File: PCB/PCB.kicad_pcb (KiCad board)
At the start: 2 copper layers, 208.3 x 169.5 mm, 307 parts, among them J55001 Debug, J60001 ALS, J60003 I2C, SW10001 SW_Push, SW11001 SW_Push, SW13001 SW_Push, SW14001 SW_Push, SW17001 SW_Push, SW18001 SW_Push, SW19001 SW_Push, SW20001 SW_Push, SW2001 SW_Push, SW21001 SW_Push, SW22001 SW_Push, SW23001 SW_Push, SW24001 SW_Push, SW25001 SW_Push, SW26001 SW_Push, SW27001 SW_Push, SW28001 SW_Push, SW30001 SW_Push, SW3001 SW_Push, SW31001 SW_Push, SW33001 SW_Push, SW34001 SW_Push, SW35001 SW_Push, SW36001 SW_Push, SW37001 SW_Push, SW38001 SW_Push, SW39001 SW_Push, SW40001 SW_Push, SW4001 SW_Push, SW41001 SW_Push, SW43001 SW_Push, SW44001 SW_Push, SW45001 SW_Push, SW46001 SW_Push, SW47001 SW_Push, SW48001 SW_Push, SW49001 SW_Push, SW50001 SW_Push, SW5001 SW_Push, SW52001 SW_Push, SW53001 SW_Push, SW56001 SW_Push, SW6001 SW_Push, SW7001 SW_Push, SW9001 SW_Push, U10001 SK6812MINI-E_C5149201, U11001 SK6812MINI-E_C5149201, U13001 SK6812MINI-E_C5149201, U14001 SK6812MINI-E_C5149201, U17001 SK6812MINI-E_C5149201, U18001 SK6812MINI-E_C5149201, U19001 SK6812MINI-E_C5149201, U20001 SK6812MINI-E_C5149201, U2001 SK6812MINI-E_C5149201, U21001 SK6812MINI-E_C5149201, U22001 SK6812MINI-E_C5149201, U23001 SK6812MINI-E_C5149201, U24001 SK6812MINI-E_C5149201, U25001 SK6812MINI-E_C5149201, U26001 SK6812MINI-E_C5149201, U27001 SK6812MINI-E_C5149201, U28001 SK6812MINI-E_C5149201, U30001 SK6812MINI-E_C5149201, U3001 SK6812MINI-E_C5149201, U31001 SK6812MINI-E_C5149201, U33001 SK6812MINI-E_C5149201, U34001 SK6812MINI-E_C5149201, U35001 SK6812MINI-E_C5149201, U36001 SK6812MINI-E_C5149201, U37001 SK6812MINI-E_C5149201, U38001 SK6812MINI-E_C5149201, U39001 SK6812MINI-E_C5149201, U40001 SK6812MINI-E_C5149201, U4001 SK6812MINI-E_C5149201, U41001 SK6812MINI-E_C5149201, U43001 SK6812MINI-E_C5149201, U44001 SK6812MINI-E_C5149201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

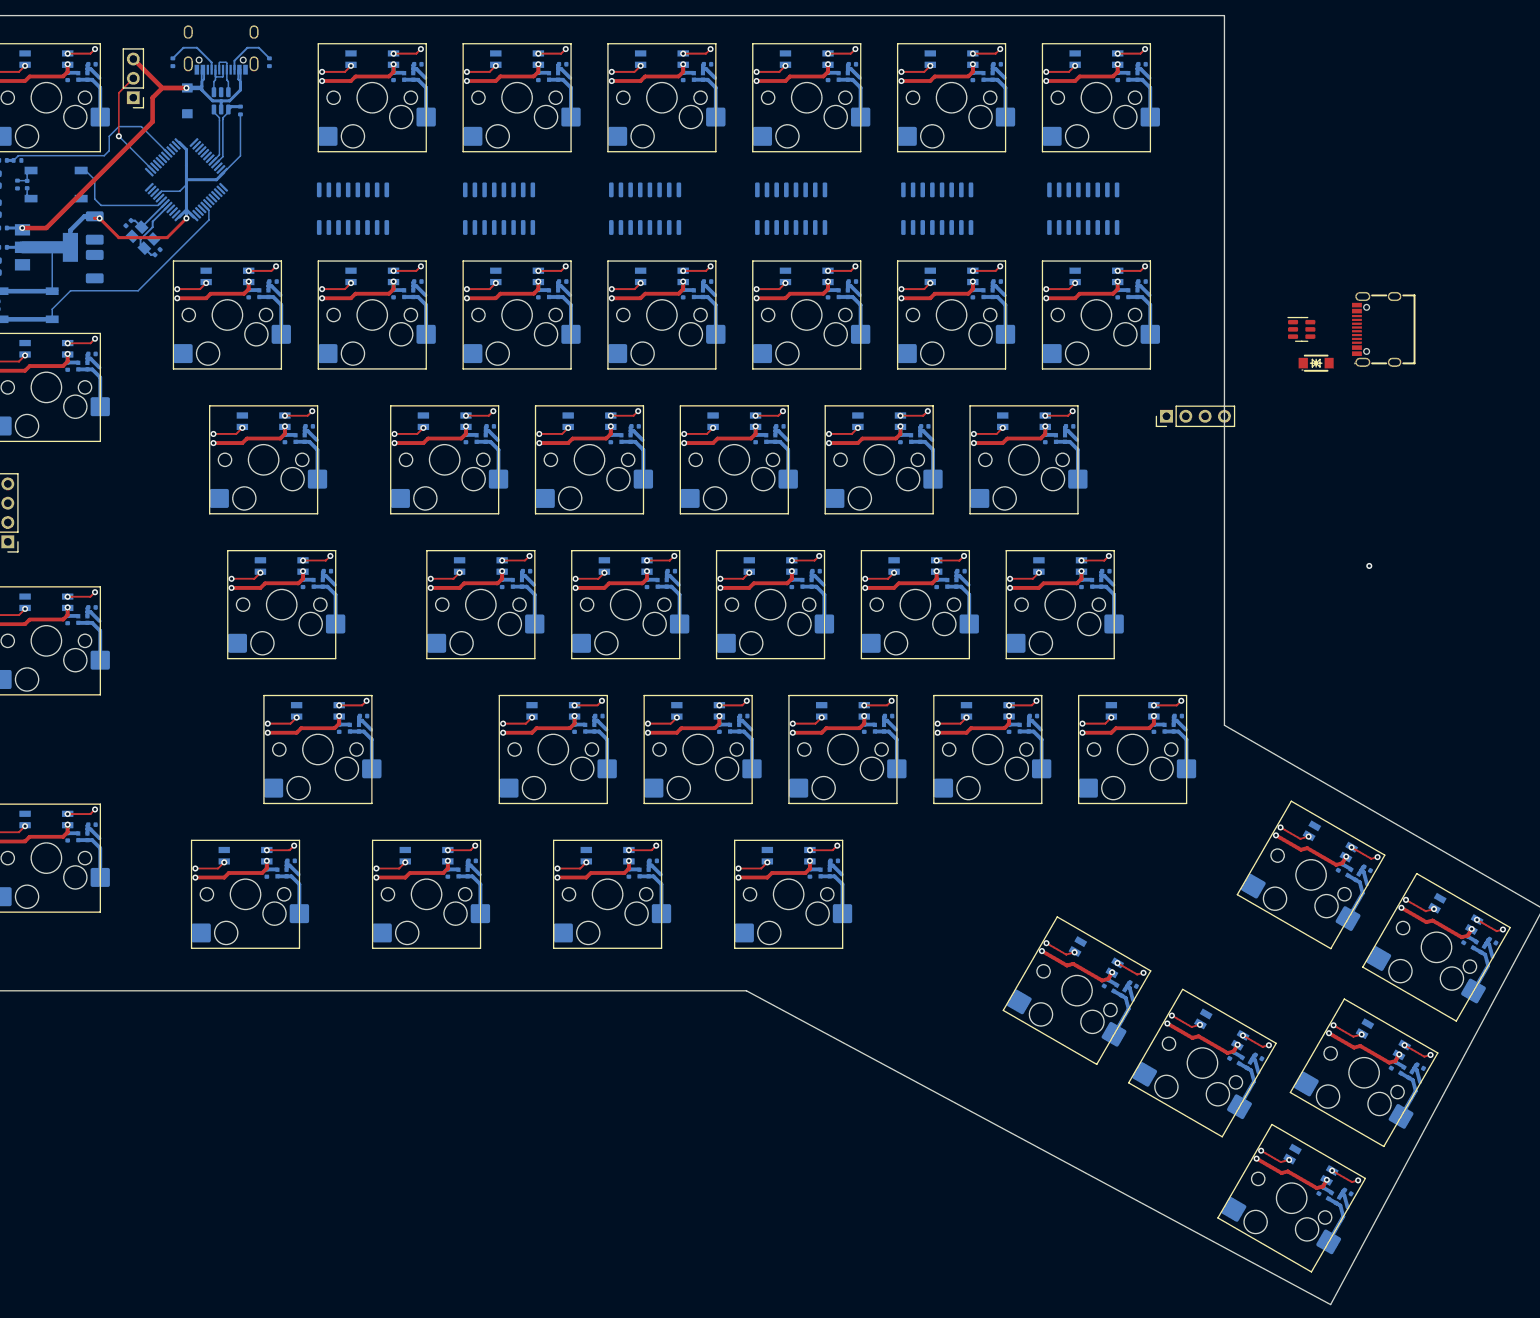
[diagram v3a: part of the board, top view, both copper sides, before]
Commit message: Removed 8-key units, now using the PCB view to handle routing the keys to the SOIP shift registers.
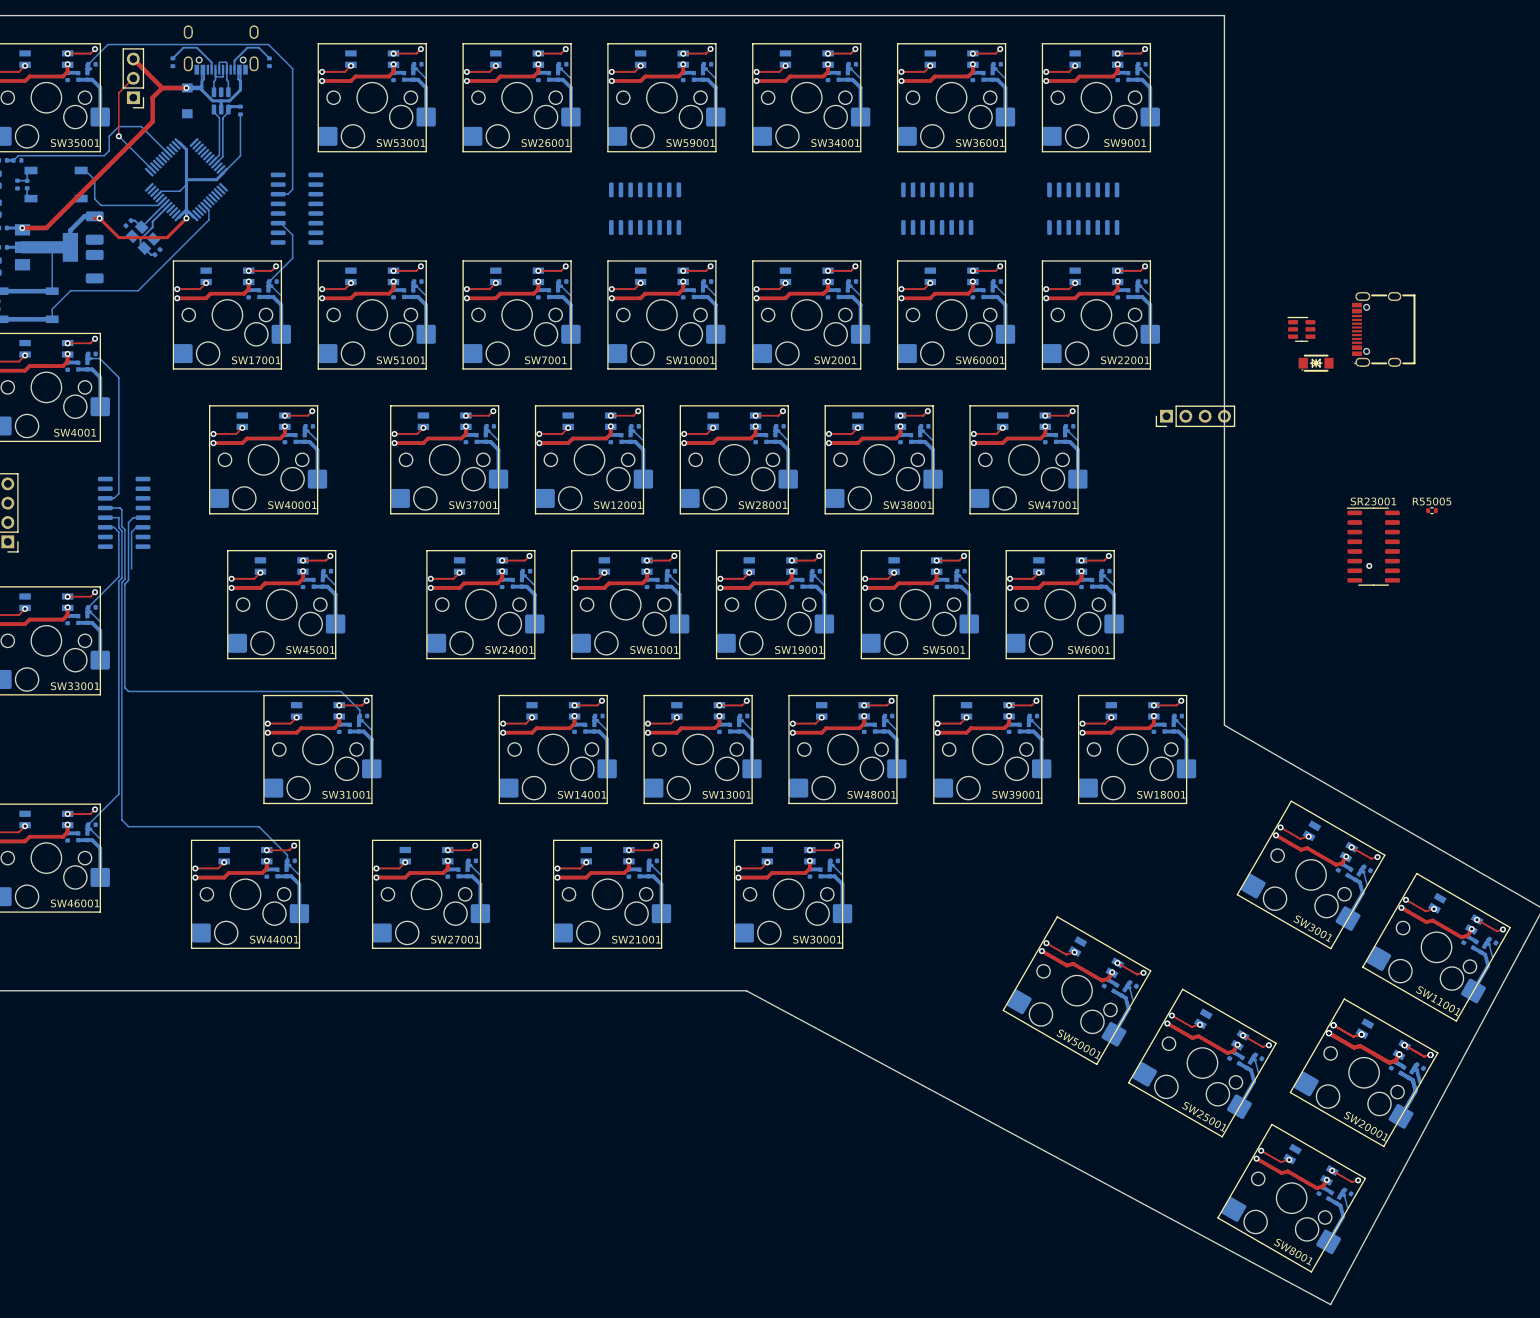
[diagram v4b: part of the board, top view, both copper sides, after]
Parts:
- removed CL23001, CL41001, CL43001, CL49001, CL52001, CL56001, CS23001, CS41001, CS43001, CS49001, CS52001, CS56001: 100nF, Capacitor_SMD:C_0402_1005Metric
- removed RA23001, RA41001, RA43001, RA49001, RA52001, RA56001: 68kΩ, footprint:R0402
- removed RB23001, RB41001, RB43001, RB49001, RB52001, RB56001: 33kΩ, footprint:R0402
- removed SR29001: 74HC165, Package_SO:SOIC-16_3.9x9.9mm_P1.27mm
- removed SW23001, SW41001, SW43001, SW49001, SW52001, SW56001: SW_Push, PCM_Switch_Keyboard_Hotswap_Kailh:SW_Hotswap_Kailh_MX
- removed U23001, U41001, U43001, U49001, U52001, U56001: SK6812MINI-E_C5149201, footprint:LED-SMD_L3.2-W2.8-TR
- added CL12001: 100nF, Capacitor_SMD:C_0402_1005Metric, B.Cu at (104.7, 75.9)
- added CL51001: 100nF, Capacitor_SMD:C_0402_1005Metric, B.Cu at (76.1, 56.9)
- added CL59001: 100nF, Capacitor_SMD:C_0402_1005Metric, B.Cu at (114.2, 28.3)
- added CL60001: 100nF, Capacitor_SMD:C_0402_1005Metric, B.Cu at (152.3, 56.9)
- added CL61001: 100nF, Capacitor_SMD:C_0402_1005Metric, B.Cu at (109.5, 95.0)
- added CL8001: 100nF, Capacitor_SMD:C_0402_1005Metric, B.Cu at (198.1, 174.8)
- added CS12001: 100nF, Capacitor_SMD:C_0402_1005Metric, B.Cu at (107.9, 74.3)
- added CS51001: 100nF, Capacitor_SMD:C_0402_1005Metric, B.Cu at (79.3, 55.3)
- added CS59001: 100nF, Capacitor_SMD:C_0402_1005Metric, B.Cu at (117.4, 26.7)
- added CS60001: 100nF, Capacitor_SMD:C_0402_1005Metric, B.Cu at (155.5, 55.3)
- added CS61001: 100nF, Capacitor_SMD:C_0402_1005Metric, B.Cu at (112.7, 93.4)
- added CS8001: 100nF, Capacitor_SMD:C_0402_1005Metric, B.Cu at (201.7, 175.1)
- added R55005: 5.1k, Resistor_SMD:R_0402_1005Metric, F.Cu at (212.7, 85.4)
- added RA12001: 68kΩ, footprint:R0402, B.Cu at (106.1, 75.9)
- added RA51001: 68kΩ, footprint:R0402, B.Cu at (77.5, 56.9)
- added RA59001: 68kΩ, footprint:R0402, B.Cu at (115.6, 28.3)
- added RA60001: 68kΩ, footprint:R0402, B.Cu at (153.7, 56.9)
- added RA61001: 68kΩ, footprint:R0402, B.Cu at (110.9, 95.0)
- added RA8001: 68kΩ, footprint:R0402, B.Cu at (199.3, 175.5)
- added RB12001: 33kΩ, footprint:R0402, B.Cu at (107.3, 75.9)
- added RB51001: 33kΩ, footprint:R0402, B.Cu at (78.7, 56.9)
- added RB59001: 33kΩ, footprint:R0402, B.Cu at (116.8, 28.3)
- added RB60001: 33kΩ, footprint:R0402, B.Cu at (154.9, 56.9)
- added RB61001: 33kΩ, footprint:R0402, B.Cu at (112.1, 95.0)
- added RB8001: 33kΩ, footprint:R0402, B.Cu at (200.3, 176.1)
- added SR23001: 74HC165, Package_SO:SOIC-16_3.9x9.9mm_P1.27mm, F.Cu at (205.0, 90.2)
- added SW12001: SW_Push, PCM_Switch_Keyboard_Hotswap_Kailh:SW_Hotswap_Kailh_MX, F.Cu at (101.9, 78.7)
- added SW51001: SW_Push, PCM_Switch_Keyboard_Hotswap_Kailh:SW_Hotswap_Kailh_MX, F.Cu at (73.3, 59.7)
- added SW59001: SW_Push, PCM_Switch_Keyboard_Hotswap_Kailh:SW_Hotswap_Kailh_MX, F.Cu at (111.4, 31.1)
- added SW60001: SW_Push, PCM_Switch_Keyboard_Hotswap_Kailh:SW_Hotswap_Kailh_MX, F.Cu at (149.5, 59.7)
- added SW61001: SW_Push, PCM_Switch_Keyboard_Hotswap_Kailh:SW_Hotswap_Kailh_MX, F.Cu at (106.7, 97.8)
- added SW8001: SW_Push, PCM_Switch_Keyboard_Hotswap_Kailh:SW_Hotswap_Kailh_MX, F.Cu at (194.3, 175.9)
- added U12001: SK6812MINI-E_C5149201, footprint:LED-SMD_L3.2-W2.8-TR, B.Cu at (101.9, 73.7)
- added U51001: SK6812MINI-E_C5149201, footprint:LED-SMD_L3.2-W2.8-TR, B.Cu at (73.3, 54.6)
- added U59001: SK6812MINI-E_C5149201, footprint:LED-SMD_L3.2-W2.8-TR, B.Cu at (111.4, 26.0)
- added U60003: SK6812MINI-E_C5149201, footprint:LED-SMD_L3.2-W2.8-TR, B.Cu at (149.5, 54.6)
- added U61001: SK6812MINI-E_C5149201, footprint:LED-SMD_L3.2-W2.8-TR, B.Cu at (106.7, 92.7)
- added U8001: SK6812MINI-E_C5149201, footprint:LED-SMD_L3.2-W2.8-TR, B.Cu at (196.8, 171.5)
- R55006: value 7.7k -> 5.1k
- moved CS4001 198.3 mm to (36.5, 64.8), turned to 180 degrees
- moved U4001 197.9 mm to (30.5, 64.1), turned to 0 degrees
- moved RB4001 197.4 mm to (35.9, 66.4), turned to -90 degrees
- moved RA4001 197.3 mm to (34.7, 66.4), turned to 90 degrees
- moved CL4001 197.1 mm to (33.3, 66.4), turned to 90 degrees
- moved SW4001 195.4 mm to (30.5, 69.2), turned to 180 degrees
- moved U3001 168.9 mm to (199.4, 128.9), turned to -30 degrees
- moved CS3001 167.8 mm to (204.2, 132.5), turned to 150 degrees
- moved CL3001 167.4 mm to (200.6, 132.3), turned to 60 degrees
- moved RA3001 167.2 mm to (201.9, 133.0), turned to 60 degrees
- moved RB3001 167.1 mm to (202.9, 133.6), turned to -120 degrees
- moved SW3001 166.4 mm to (196.8, 133.3), turned to 150 degrees
- moved U20001 146.6 mm to (206.3, 155.0), turned to -30 degrees
- moved CS20001 146.4 mm to (211.2, 158.6), turned to 150 degrees
- moved RB20001 145.6 mm to (209.9, 159.6), turned to -120 degrees
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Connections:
- net /Left Half/5-Key Module/SR_CLOCK renamed /Left Half/8-Key Module/SR_CLOCK
- net /Left Half/5-Key Module/SR_LOAD renamed /Left Half/8-Key Module/SR_LOAD
- CS10001 pad 2: /Left Half/8-Key Module4/Key Unit1/SwitchOutput -> /Left Half/Key Unit16/SwitchOutput
- CS11001 pad 2: /Left Half/8-Key Module1/Key Unit6/SwitchOutput -> /Left Half/Key Unit20/SwitchOutput
- CS13001 pad 2: /Left Half/8-Key Module3/Key Unit4/SwitchOutput -> /Left Half/Key Unit18/SwitchOutput
- CS14001 pad 2: /Left Half/8-Key Module/Key Unit7/SwitchOutput -> /Left Half/Key Unit14/SwitchOutput
- CS17001 pad 2: /Left Half/8-Key Module3/Key Unit3/SwitchOutput -> /Left Half/Key Unit15/SwitchOutput
- CS18001 pad 2: /Left Half/8-Key Module3/Key Unit5/SwitchOutput -> /Left Half/Key Unit11/SwitchOutput
- CS19001 pad 2: /Left Half/8-Key Module4/Key Unit4/SwitchOutput -> /Left Half/Key Unit17/SwitchOutput
- CS20001 pad 2: /Left Half/8-Key Module3/Key Unit2/SwitchOutput -> /Left Half/Key Unit24/SwitchOutput
- CS2001 pad 2: /Left Half/8-Key Module1/Key Unit7/SwitchOutput -> /Left Half/Key Unit6/SwitchOutput
- CS21001 pad 2: /Left Half/8-Key Module2/Key Unit5/SwitchOutput -> /Left Half/Key Unit23/SwitchOutput
- CS22001 pad 2: /Left Half/8-Key Module4/Key Unit5/SwitchOutput -> /Left Half/Key Unit22/SwitchOutput
- CS24001 pad 2: /Left Half/8-Key Module1/Key Unit5/SwitchOutput -> /Left Half/Key Unit25/SwitchOutput
- CS25001 pad 2: /Left Half/8-Key Module/Key Unit5/SwitchOutput -> /Left Half/Key Unit27/SwitchOutput
- CS26001 pad 2: /Left Half/8-Key Module1/Key Unit4/SwitchOutput -> /Left Half/Key Unit21/SwitchOutput
- CS27001 pad 2: /Left Half/8-Key Module4/Key Unit0/SwitchOutput -> /Left Half/Key Unit26/SwitchOutput
- CS28001 pad 2: /Left Half/8-Key Module3/Key Unit6/SwitchOutput -> /Left Half/Key Unit28/SwitchOutput
- CS30001 pad 2: /Left Half/8-Key Module2/Key Unit2/SwitchOutput -> /Left Half/Key Unit30/SwitchOutput
- CS3001 pad 2: /Left Half/8-Key Module4/Key Unit3/SwitchOutput -> /Left Half/Key Unit7/SwitchOutput
- CS31001 pad 2: /Left Half/8-Key Module2/Key Unit1/SwitchOutput -> /Left Half/Key Unit34/SwitchOutput
- CS33001 pad 2: /Left Half/8-Key Module3/Key Unit7/SwitchOutput -> /Left Half/Key Unit33/SwitchOutput
- CS34001 pad 2: /Left Half/8-Key Module1/Key Unit3/SwitchOutput -> /Left Half/Key Unit35/SwitchOutput
- CS35001 pad 2: /Left Half/8-Key Module4/Key Unit6/SwitchOutput -> /Left Half/8-Key Module2/SWIN1
- CS36001 pad 2: /Left Half/8-Key Module3/Key Unit1/SwitchOutput -> /Left Half/Key Unit29/SwitchOutput
- CS37001 pad 2: /Left Half/8-Key Module2/Key Unit3/SwitchOutput -> /Left Half/Key Unit32/SwitchOutput
- CS38001 pad 2: /Left Half/8-Key Module/Key Unit3/SwitchOutput -> /Left Half/Key Unit36/SwitchOutput
- CS39001 pad 2: /Left Half/8-Key Module2/Key Unit4/SwitchOutput -> /Left Half/Key Unit37/SwitchOutput
- CS40001 pad 2: /Left Half/8-Key Module/Key Unit0/SwitchOutput -> /Left Half/Key Unit42/SwitchOutput
- CS4001 pad 2: /Left Half/8-Key Module/Key Unit2/SwitchOutput -> /Left Half/Key Unit3/SwitchOutput
- CS44001 pad 2: /Left Half/8-Key Module3/Key Unit0/SwitchOutput -> /Left Half/Key Unit43/SwitchOutput
- CS45001 pad 2: /Left Half/8-Key Module1/Key Unit1/SwitchOutput -> /Left Half/Key Unit44/SwitchOutput
- CS46001 pad 2: /Left Half/8-Key Module2/Key Unit7/SwitchOutput -> /Left Half/Key Unit38/SwitchOutput
- CS47001 pad 2: /Left Half/8-Key Module4/Key Unit7/SwitchOutput -> /Left Half/Key Unit39/SwitchOutput
- CS48001 pad 2: /Left Half/8-Key Module4/Key Unit2/SwitchOutput -> /Left Half/Key Unit41/SwitchOutput
- CS50001 pad 2: /Left Half/8-Key Module/Key Unit6/SwitchOutput -> /Left Half/Key Unit40/SwitchOutput
- CS5001 pad 2: /Left Half/8-Key Module2/Key Unit6/SwitchOutput -> /Left Half/Key Unit1/SwitchOutput
- CS53001 pad 2: /Left Half/8-Key Module1/Key Unit2/SwitchOutput -> /Left Half/Key Unit45/SwitchOutput
- CS6001 pad 2: /Left Half/8-Key Module2/Key Unit0/SwitchOutput -> /Left Half/Key Unit5/SwitchOutput
- CS7001 pad 2: /Left Half/8-Key Module1/Key Unit0/SwitchOutput -> /Left Half/Key Unit4/SwitchOutput
- CS9001 pad 2: /Left Half/8-Key Module/Key Unit1/SwitchOutput -> /Left Half/Key Unit0/SwitchOutput
- R55006 pad 1: +5V -> Net-(R55005-Pad2)
- RB10001 pad 1: /Left Half/8-Key Module4/Key Unit1/SwitchOutput -> /Left Half/Key Unit16/SwitchOutput
- RB11001 pad 1: /Left Half/8-Key Module1/Key Unit6/SwitchOutput -> /Left Half/Key Unit20/SwitchOutput
- RB13001 pad 1: /Left Half/8-Key Module3/Key Unit4/SwitchOutput -> /Left Half/Key Unit18/SwitchOutput
- RB14001 pad 1: /Left Half/8-Key Module/Key Unit7/SwitchOutput -> /Left Half/Key Unit14/SwitchOutput
- RB17001 pad 1: /Left Half/8-Key Module3/Key Unit3/SwitchOutput -> /Left Half/Key Unit15/SwitchOutput
- RB18001 pad 1: /Left Half/8-Key Module3/Key Unit5/SwitchOutput -> /Left Half/Key Unit11/SwitchOutput
- RB19001 pad 1: /Left Half/8-Key Module4/Key Unit4/SwitchOutput -> /Left Half/Key Unit17/SwitchOutput
- RB20001 pad 1: /Left Half/8-Key Module3/Key Unit2/SwitchOutput -> /Left Half/Key Unit24/SwitchOutput
- RB2001 pad 1: /Left Half/8-Key Module1/Key Unit7/SwitchOutput -> /Left Half/Key Unit6/SwitchOutput
- RB21001 pad 1: /Left Half/8-Key Module2/Key Unit5/SwitchOutput -> /Left Half/Key Unit23/SwitchOutput
- RB22001 pad 1: /Left Half/8-Key Module4/Key Unit5/SwitchOutput -> /Left Half/Key Unit22/SwitchOutput
- RB24001 pad 1: /Left Half/8-Key Module1/Key Unit5/SwitchOutput -> /Left Half/Key Unit25/SwitchOutput
- RB25001 pad 1: /Left Half/8-Key Module/Key Unit5/SwitchOutput -> /Left Half/Key Unit27/SwitchOutput
- RB26001 pad 1: /Left Half/8-Key Module1/Key Unit4/SwitchOutput -> /Left Half/Key Unit21/SwitchOutput
- RB27001 pad 1: /Left Half/8-Key Module4/Key Unit0/SwitchOutput -> /Left Half/Key Unit26/SwitchOutput
- RB28001 pad 1: /Left Half/8-Key Module3/Key Unit6/SwitchOutput -> /Left Half/Key Unit28/SwitchOutput
- RB30001 pad 1: /Left Half/8-Key Module2/Key Unit2/SwitchOutput -> /Left Half/Key Unit30/SwitchOutput
- RB3001 pad 1: /Left Half/8-Key Module4/Key Unit3/SwitchOutput -> /Left Half/Key Unit7/SwitchOutput
- RB31001 pad 1: /Left Half/8-Key Module2/Key Unit1/SwitchOutput -> /Left Half/Key Unit34/SwitchOutput
- RB33001 pad 1: /Left Half/8-Key Module3/Key Unit7/SwitchOutput -> /Left Half/Key Unit33/SwitchOutput
- RB34001 pad 1: /Left Half/8-Key Module1/Key Unit3/SwitchOutput -> /Left Half/Key Unit35/SwitchOutput
- RB35001 pad 1: /Left Half/8-Key Module4/Key Unit6/SwitchOutput -> /Left Half/8-Key Module2/SWIN1
- RB36001 pad 1: /Left Half/8-Key Module3/Key Unit1/SwitchOutput -> /Left Half/Key Unit29/SwitchOutput
- RB37001 pad 1: /Left Half/8-Key Module2/Key Unit3/SwitchOutput -> /Left Half/Key Unit32/SwitchOutput
- RB38001 pad 1: /Left Half/8-Key Module/Key Unit3/SwitchOutput -> /Left Half/Key Unit36/SwitchOutput
- RB39001 pad 1: /Left Half/8-Key Module2/Key Unit4/SwitchOutput -> /Left Half/Key Unit37/SwitchOutput
- RB40001 pad 1: /Left Half/8-Key Module/Key Unit0/SwitchOutput -> /Left Half/Key Unit42/SwitchOutput
- RB4001 pad 1: /Left Half/8-Key Module/Key Unit2/SwitchOutput -> /Left Half/Key Unit3/SwitchOutput
- RB44001 pad 1: /Left Half/8-Key Module3/Key Unit0/SwitchOutput -> /Left Half/Key Unit43/SwitchOutput
- RB45001 pad 1: /Left Half/8-Key Module1/Key Unit1/SwitchOutput -> /Left Half/Key Unit44/SwitchOutput
- RB46001 pad 1: /Left Half/8-Key Module2/Key Unit7/SwitchOutput -> /Left Half/Key Unit38/SwitchOutput
- RB47001 pad 1: /Left Half/8-Key Module4/Key Unit7/SwitchOutput -> /Left Half/Key Unit39/SwitchOutput
- RB48001 pad 1: /Left Half/8-Key Module4/Key Unit2/SwitchOutput -> /Left Half/Key Unit41/SwitchOutput
- RB50001 pad 1: /Left Half/8-Key Module/Key Unit6/SwitchOutput -> /Left Half/Key Unit40/SwitchOutput
- RB5001 pad 1: /Left Half/8-Key Module2/Key Unit6/SwitchOutput -> /Left Half/Key Unit1/SwitchOutput
- RB53001 pad 1: /Left Half/8-Key Module1/Key Unit2/SwitchOutput -> /Left Half/Key Unit45/SwitchOutput
- RB6001 pad 1: /Left Half/8-Key Module2/Key Unit0/SwitchOutput -> /Left Half/Key Unit5/SwitchOutput
- RB7001 pad 1: /Left Half/8-Key Module1/Key Unit0/SwitchOutput -> /Left Half/Key Unit4/SwitchOutput
- RB9001 pad 1: /Left Half/8-Key Module/Key Unit1/SwitchOutput -> /Left Half/Key Unit0/SwitchOutput
- SR15001 pad 11: /Left Half/8-Key Module2/Key Unit7/SwitchOutput -> /Left Half/8-Key Module2/SWIN8
- SR15001 pad 12: /Left Half/8-Key Module2/Key Unit6/SwitchOutput -> /Left Half/8-Key Module2/SWIN7
- SR15001 pad 13: /Left Half/8-Key Module2/Key Unit5/SwitchOutput -> /Left Half/8-Key Module2/SWIN6
- SR15001 pad 14: /Left Half/8-Key Module2/Key Unit4/SwitchOutput -> /Left Half/8-Key Module2/SWIN5
- SR15001 pad 3: /Left Half/8-Key Module2/Key Unit3/SwitchOutput -> /Left Half/Key Unit15/SwitchOutput
- SR15001 pad 4: /Left Half/8-Key Module2/Key Unit2/SwitchOutput -> /Left Half/8-Key Module2/SWIN3
- SR15001 pad 5: /Left Half/8-Key Module2/Key Unit1/SwitchOutput -> /Left Half/8-Key Module2/SWIN2
- SR15001 pad 6: /Left Half/8-Key Module2/Key Unit0/SwitchOutput -> /Left Half/8-Key Module2/SWIN1
- SR16001 pad 11: /Left Half/8-Key Module3/Key Unit7/SwitchOutput -> /Left Half/8-Key Module3/SWIN8
- SR16001 pad 12: /Left Half/8-Key Module3/Key Unit6/SwitchOutput -> /Left Half/8-Key Module3/SWIN7
- SR16001 pad 13: /Left Half/8-Key Module3/Key Unit5/SwitchOutput -> /Left Half/8-Key Module3/SWIN6
- SR16001 pad 14: /Left Half/8-Key Module3/Key Unit4/SwitchOutput -> /Left Half/8-Key Module3/SWIN5
- SR16001 pad 3: /Left Half/8-Key Module3/Key Unit3/SwitchOutput -> /Left Half/8-Key Module3/SWIN4
- SR16001 pad 4: /Left Half/8-Key Module3/Key Unit2/SwitchOutput -> /Left Half/8-Key Module3/SWIN3
- SR16001 pad 5: /Left Half/8-Key Module3/Key Unit1/SwitchOutput -> /Left Half/8-Key Module3/SWIN2
- SR16001 pad 6: /Left Half/8-Key Module3/Key Unit0/SwitchOutput -> /Left Half/8-Key Module3/SWIN1
- SR32001 pad 11: /Left Half/8-Key Module4/Key Unit7/SwitchOutput -> /Left Half/8-Key Module4/SWIN8
- SR32001 pad 12: /Left Half/8-Key Module4/Key Unit6/SwitchOutput -> /Left Half/8-Key Module4/SWIN7
- SR32001 pad 13: /Left Half/8-Key Module4/Key Unit5/SwitchOutput -> /Left Half/8-Key Module4/SWIN6
- SR32001 pad 14: /Left Half/8-Key Module4/Key Unit4/SwitchOutput -> /Left Half/8-Key Module4/SWIN5
- SR32001 pad 3: /Left Half/8-Key Module4/Key Unit3/SwitchOutput -> /Left Half/8-Key Module4/SWIN4
- SR32001 pad 4: /Left Half/8-Key Module4/Key Unit2/SwitchOutput -> /Left Half/8-Key Module4/SWIN3
- SR32001 pad 5: /Left Half/8-Key Module4/Key Unit1/SwitchOutput -> /Left Half/8-Key Module4/SWIN2
- SR32001 pad 6: /Left Half/8-Key Module4/Key Unit0/SwitchOutput -> /Left Half/8-Key Module4/SWIN1
- SR32001 pad 9: /Left Half/5-Key Module/SR_IN -> /Left Half/8-Key Module4/SR_OUT
- SR42001 pad 11: /Left Half/8-Key Module1/Key Unit7/SwitchOutput -> /Left Half/8-Key Module1/SWIN8
- SR42001 pad 12: /Left Half/8-Key Module1/Key Unit6/SwitchOutput -> /Left Half/8-Key Module1/SWIN7
- SR42001 pad 13: /Left Half/8-Key Module1/Key Unit5/SwitchOutput -> /Left Half/8-Key Module1/SWIN6
- SR42001 pad 14: /Left Half/8-Key Module1/Key Unit4/SwitchOutput -> /Left Half/8-Key Module1/SWIN5
- SR42001 pad 3: /Left Half/8-Key Module1/Key Unit3/SwitchOutput -> /Left Half/8-Key Module1/SWIN4
- SR42001 pad 4: /Left Half/8-Key Module1/Key Unit2/SwitchOutput -> /Left Half/8-Key Module1/SWIN3
- SR42001 pad 5: /Left Half/8-Key Module1/Key Unit1/SwitchOutput -> /Left Half/8-Key Module1/SWIN2
- SR42001 pad 6: /Left Half/8-Key Module1/Key Unit0/SwitchOutput -> /Left Half/8-Key Module1/SWIN1
- SR54001 pad 11: /Left Half/8-Key Module/Key Unit7/SwitchOutput -> /Left Half/Key Unit33/SwitchOutput
- SR54001 pad 12: /Left Half/8-Key Module/Key Unit6/SwitchOutput -> /Left Half/Key Unit38/SwitchOutput
- SR54001 pad 13: /Left Half/8-Key Module/Key Unit5/SwitchOutput -> /Left Half/Key Unit43/SwitchOutput
- SR54001 pad 14: /Left Half/8-Key Module/Key Unit4/SwitchOutput -> /Left Half/Key Unit3/SwitchOutput
- SR54001 pad 3: /Left Half/8-Key Module/Key Unit3/SwitchOutput -> /Left Half/8-Key Module/SWIN4
- SR54001 pad 4: /Left Half/8-Key Module/Key Unit2/SwitchOutput -> /Left Half/8-Key Module/SWIN3
- SR54001 pad 5: /Left Half/8-Key Module/Key Unit1/SwitchOutput -> /Left Half/Key Unit34/SwitchOutput
- SR54001 pad 6: /Left Half/8-Key Module/Key Unit0/SwitchOutput -> /Left Half/8-Key Module/SWIN1
- STM55001 pad 38: /Left Half/5-Key Module/SR_OUT -> /Left Half/8-Key Module5/SR_OUT
- STM55001 pad 39: /Left Half/8-Key Module/LEDInput -> /Left Half/LEDInput
- U10001 pad 2: /Left Half/8-Key Module4/Key Unit1/LEDOutput -> /Left Half/Key Unit16/LEDOutput
- U10001 pad 4: /Left Half/8-Key Module4/Key Unit0/LEDOutput -> /Left Half/Key Unit16/LEDInput
- U11001 pad 2: /Left Half/8-Key Module1/Key Unit6/LEDOutput -> /Left Half/Key Unit20/LEDOutput
- U11001 pad 4: /Left Half/8-Key Module1/Key Unit5/LEDOutput -> /Left Half/Key Unit20/LEDInput
- U13001 pad 2: /Left Half/8-Key Module3/Key Unit4/LEDOutput -> /Left Half/Key Unit18/LEDOutput
- U13001 pad 4: /Left Half/8-Key Module3/Key Unit3/LEDOutput -> /Left Half/Key Unit18/LEDInput
- U14001 pad 2: /Left Half/8-Key Module/LEDOutput -> /Left Half/Key Unit14/LEDOutput
- U14001 pad 4: /Left Half/8-Key Module/Key Unit6/LEDOutput -> /Left Half/Key Unit14/LEDInput
- U17001 pad 2: /Left Half/8-Key Module3/Key Unit3/LEDOutput -> /Left Half/Key Unit15/LEDOutput
- U17001 pad 4: /Left Half/8-Key Module3/Key Unit2/LEDOutput -> /Left Half/Key Unit15/LEDInput
- U18001 pad 2: /Left Half/8-Key Module3/Key Unit5/LEDOutput -> /Left Half/Key Unit11/LEDOutput
- U18001 pad 4: /Left Half/8-Key Module3/Key Unit4/LEDOutput -> /Left Half/Key Unit11/LEDInput
- U19001 pad 2: /Left Half/8-Key Module4/Key Unit4/LEDOutput -> /Left Half/Key Unit17/LEDOutput
- U19001 pad 4: /Left Half/8-Key Module4/Key Unit3/LEDOutput -> /Left Half/Key Unit17/LEDInput
- U20001 pad 2: /Left Half/8-Key Module3/Key Unit2/LEDOutput -> /Left Half/Key Unit24/LEDOutput
- U20001 pad 4: /Left Half/8-Key Module3/Key Unit1/LEDOutput -> /Left Half/Key Unit24/LEDInput
- U2001 pad 2: /Left Half/8-Key Module1/LEDOutput -> /Left Half/Key Unit6/LEDOutput
- U2001 pad 4: /Left Half/8-Key Module1/Key Unit6/LEDOutput -> /Left Half/Key Unit6/LEDInput
- U21001 pad 2: /Left Half/8-Key Module2/Key Unit5/LEDOutput -> /Left Half/Key Unit23/LEDOutput
- U21001 pad 4: /Left Half/8-Key Module2/Key Unit4/LEDOutput -> /Left Half/Key Unit23/LEDInput
- U22001 pad 2: /Left Half/8-Key Module4/Key Unit5/LEDOutput -> /Left Half/Key Unit22/LEDOutput
- U22001 pad 4: /Left Half/8-Key Module4/Key Unit4/LEDOutput -> /Left Half/Key Unit22/LEDInput
- U24001 pad 2: /Left Half/8-Key Module1/Key Unit5/LEDOutput -> /Left Half/Key Unit25/LEDOutput
- U24001 pad 4: /Left Half/8-Key Module1/Key Unit4/LEDOutput -> /Left Half/Key Unit25/LEDInput
- U25001 pad 2: /Left Half/8-Key Module/Key Unit5/LEDOutput -> /Left Half/Key Unit27/LEDOutput
- U25001 pad 4: /Left Half/8-Key Module/Key Unit4/LEDOutput -> /Left Half/Key Unit27/LEDInput
- U26001 pad 2: /Left Half/8-Key Module1/Key Unit4/LEDOutput -> /Left Half/Key Unit21/LEDOutput
- U26001 pad 4: /Left Half/8-Key Module1/Key Unit3/LEDOutput -> /Left Half/Key Unit21/LEDInput
- U27001 pad 2: /Left Half/8-Key Module4/Key Unit0/LEDOutput -> /Left Half/Key Unit26/LEDOutput
- U27001 pad 4: /Left Half/8-Key Module3/LEDOutput -> /Left Half/Key Unit26/LEDInput
- U28001 pad 2: /Left Half/8-Key Module3/Key Unit6/LEDOutput -> /Left Half/Key Unit28/LEDOutput
- U28001 pad 4: /Left Half/8-Key Module3/Key Unit5/LEDOutput -> /Left Half/Key Unit28/LEDInput
- U30001 pad 2: /Left Half/8-Key Module2/Key Unit2/LEDOutput -> /Left Half/Key Unit30/LEDOutput
- U30001 pad 4: /Left Half/8-Key Module2/Key Unit1/LEDOutput -> /Left Half/Key Unit30/LEDInput
- U3001 pad 2: /Left Half/8-Key Module4/Key Unit3/LEDOutput -> /Left Half/Key Unit7/LEDOutput
- U3001 pad 4: /Left Half/8-Key Module4/Key Unit2/LEDOutput -> /Left Half/Key Unit7/LEDInput
- U31001 pad 2: /Left Half/8-Key Module2/Key Unit1/LEDOutput -> /Left Half/Key Unit34/LEDOutput
- U31001 pad 4: /Left Half/8-Key Module2/Key Unit0/LEDOutput -> /Left Half/Key Unit34/LEDInput
- U33001 pad 2: /Left Half/8-Key Module3/LEDOutput -> /Left Half/Key Unit33/LEDOutput
- U33001 pad 4: /Left Half/8-Key Module3/Key Unit6/LEDOutput -> /Left Half/Key Unit33/LEDInput
- U34001 pad 2: /Left Half/8-Key Module1/Key Unit3/LEDOutput -> /Left Half/Key Unit35/LEDOutput
- U34001 pad 4: /Left Half/8-Key Module1/Key Unit2/LEDOutput -> /Left Half/Key Unit35/LEDInput
- U35001 pad 2: /Left Half/8-Key Module4/Key Unit6/LEDOutput -> /Left Half/Key Unit31/LEDOutput
- U35001 pad 4: /Left Half/8-Key Module4/Key Unit5/LEDOutput -> /Left Half/Key Unit31/LEDInput
- U36001 pad 2: /Left Half/8-Key Module3/Key Unit1/LEDOutput -> /Left Half/Key Unit29/LEDOutput
- U36001 pad 4: /Left Half/8-Key Module3/Key Unit0/LEDOutput -> /Left Half/Key Unit29/LEDInput
- U37001 pad 2: /Left Half/8-Key Module2/Key Unit3/LEDOutput -> /Left Half/Key Unit32/LEDOutput
- U37001 pad 4: /Left Half/8-Key Module2/Key Unit2/LEDOutput -> /Left Half/Key Unit32/LEDInput
- U38001 pad 2: /Left Half/8-Key Module/Key Unit3/LEDOutput -> /Left Half/Key Unit36/LEDOutput
- U38001 pad 4: /Left Half/8-Key Module/Key Unit2/LEDOutput -> /Left Half/Key Unit36/LEDInput
- U39001 pad 2: /Left Half/8-Key Module2/Key Unit4/LEDOutput -> /Left Half/Key Unit37/LEDOutput
- U39001 pad 4: /Left Half/8-Key Module2/Key Unit3/LEDOutput -> /Left Half/Key Unit37/LEDInput
- U40001 pad 2: /Left Half/8-Key Module/Key Unit0/LEDOutput -> /Left Half/Key Unit42/LEDOutput
- U40001 pad 4: /Left Half/8-Key Module/LEDInput -> /Left Half/Key Unit42/LEDInput
- U4001 pad 2: /Left Half/8-Key Module/Key Unit2/LEDOutput -> /Left Half/Key Unit3/LEDOutput
- U4001 pad 4: /Left Half/8-Key Module/Key Unit1/LEDOutput -> /Left Half/Key Unit3/LEDInput
- U44001 pad 2: /Left Half/8-Key Module3/Key Unit0/LEDOutput -> /Left Half/Key Unit43/LEDOutput
- U44001 pad 4: /Left Half/8-Key Module2/LEDOutput -> /Left Half/Key Unit43/LEDInput
- U45001 pad 2: /Left Half/8-Key Module1/Key Unit1/LEDOutput -> /Left Half/Key Unit44/LEDOutput
- U45001 pad 4: /Left Half/8-Key Module1/Key Unit0/LEDOutput -> /Left Half/Key Unit44/LEDInput
- U46001 pad 2: /Left Half/8-Key Module2/LEDOutput -> /Left Half/Key Unit38/LEDOutput
- U46001 pad 4: /Left Half/8-Key Module2/Key Unit6/LEDOutput -> /Left Half/Key Unit38/LEDInput
- U47001 pad 2: /Left Half/5-Key Module/LEDInput -> /Left Half/Key Unit39/LEDOutput
- U47001 pad 4: /Left Half/8-Key Module4/Key Unit6/LEDOutput -> /Left Half/Key Unit39/LEDInput
- U48001 pad 2: /Left Half/8-Key Module4/Key Unit2/LEDOutput -> /Left Half/Key Unit41/LEDOutput
- U48001 pad 4: /Left Half/8-Key Module4/Key Unit1/LEDOutput -> /Left Half/Key Unit41/LEDInput
- U50001 pad 2: /Left Half/8-Key Module/Key Unit6/LEDOutput -> /Left Half/Key Unit40/LEDOutput
- U50001 pad 4: /Left Half/8-Key Module/Key Unit5/LEDOutput -> /Left Half/Key Unit40/LEDInput
- U5001 pad 2: /Left Half/8-Key Module2/Key Unit6/LEDOutput -> /Left Half/Key Unit1/LEDOutput
- U5001 pad 4: /Left Half/8-Key Module2/Key Unit5/LEDOutput -> /Left Half/Key Unit1/LEDInput
- U53001 pad 2: /Left Half/8-Key Module1/Key Unit2/LEDOutput -> /Left Half/Key Unit45/LEDOutput
- U53001 pad 4: /Left Half/8-Key Module1/Key Unit1/LEDOutput -> /Left Half/Key Unit45/LEDInput
- U6001 pad 2: /Left Half/8-Key Module2/Key Unit0/LEDOutput -> /Left Half/Key Unit5/LEDOutput
- U6001 pad 4: /Left Half/8-Key Module1/LEDOutput -> /Left Half/Key Unit5/LEDInput
- U7001 pad 2: /Left Half/8-Key Module1/Key Unit0/LEDOutput -> /Left Half/Key Unit4/LEDOutput
- U7001 pad 4: /Left Half/8-Key Module/LEDOutput -> /Left Half/Key Unit4/LEDInput
- U9001 pad 2: /Left Half/8-Key Module/Key Unit1/LEDOutput -> /Left Half/Key Unit0/LEDOutput
- U9001 pad 4: /Left Half/8-Key Module/Key Unit0/LEDOutput -> /Left Half/Key Unit0/LEDInput
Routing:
- net /Left Half/Key Unit43/SwitchOutput: track 0.00 -> 71.2 mm
- net /Left Half/Key Unit34/SwitchOutput: track 0.00 -> 60.3 mm
- net /Left Half/8-Key Module2/SWIN1: track 0.00 -> 48.9 mm
- net /Left Half/Key Unit38/SwitchOutput: track 0.00 -> 47.5 mm
- net /Left Half/Key Unit3/SwitchOutput: track 0.00 -> 23.7 mm
- net /Left Half/Key Unit33/SwitchOutput: track 0.00 -> 16.9 mm
- net +5V: track 665.3 -> 678.8 mm, vias 92 -> 94
- net /Left Half/Key Unit15/SwitchOutput: track 0.00 -> 13.2 mm
- net /Left Half/8-Key Module4/Key Unit5/LEDOutput: track 8.26 -> 0.00 mm, vias 4 -> 0
- net /Left Half/8-Key Module1/Key Unit4/LEDOutput: track 8.26 -> 0.00 mm, vias 4 -> 0
- net /Left Half/8-Key Module3/LEDOutput: track 8.26 -> 0.00 mm, vias 4 -> 0
- net /Left Half/8-Key Module3/Key Unit1/LEDOutput: track 8.26 -> 0.00 mm, vias 4 -> 0
- net /Left Half/8-Key Module3/Key Unit0/LEDOutput: track 8.26 -> 0.00 mm, vias 4 -> 0
- net /Left Half/8-Key Module2/LEDOutput: track 8.26 -> 0.00 mm, vias 4 -> 0
- net /Left Half/8-Key Module4/Key Unit6/LEDOutput: track 8.26 -> 0.00 mm, vias 4 -> 0
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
